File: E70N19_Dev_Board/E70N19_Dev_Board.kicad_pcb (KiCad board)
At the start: 2 copper layers, 71 parts, among them J1 USB_microB_2040002-1, J2 Battery 1x2, J3 JTAGSEL_JUMPER 1x3, J4 UART_PROG 1x2, J5 ERASE_JUMPER 1x3, J6 ARM-Cortex-Debug-10, J7 CAN 1x2, J8 Conn_02x15_Counter_Clockwise, J9 Conn_02x15_Counter_Clockwise, SW1 NRST_BUTTON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

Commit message: Added debug LEDs
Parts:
- added D4: LED_Small, LEDs:LED_0805, F.Cu at (142.2, 90.3)
- added D5: LED_Small, LEDs:LED_0805, F.Cu at (138.4, 90.3)
- added D6: LED_Small, LEDs:LED_0805, F.Cu at (146.1, 90.3)
- added R16: 1K, Resistors_SMD:R_0603, F.Cu at (142.2, 94.5)
- added R17: 1K, Resistors_SMD:R_0603, F.Cu at (138.4, 94.5)
- added R18: 1K, Resistors_SMD:R_0603, F.Cu at (146.1, 94.5)
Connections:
- C1 pad 1: Net-(C1-Pad1) -> /VBUS
- C2 pad 1: Net-(C1-Pad1) -> /VBUS
- C4 pad 1: Net-(C1-Pad1) -> /VBUS
- D1 pad 2: Net-(C1-Pad1) -> /VBUS
- J1 pad 1: Net-(C1-Pad1) -> /VBUS
- J8 pad 24: /PD24 -> /PD27
- J8 pad 25: /PD25 -> /PD31
- J8 pad 26: /PD26 -> GND
- J8 pad 27: /PD27 -> GND
- J8 pad 28: /PD31 -> GND
- J8 pad 29: Net-(J8-Pad29) -> /VBUS
- J8 pad 30: Net-(J8-Pad30) -> +3V3
- U1 pad 4: Net-(C1-Pad1) -> /VBUS
- U2 pad 8: Net-(C1-Pad1) -> /VBUS
- U4 pad 35: /PD25 -> Net-(D5-Pad2)
- U4 pad 36: /PD26 -> Net-(D6-Pad2)
- U4 pad 37: /PD24 -> Net-(D4-Pad2)

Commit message: Initial routing
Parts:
- moved J4 42.2 mm to (150.9, 72.4), turned to 180 degrees
- moved J8 36.9 mm to (92.2, 98.6), turned to 90 degrees
- moved R13 34.2 mm to (125.7, 43.2)
- moved D1 32.7 mm to (88.9, 37.5), turned to 270 degrees
- moved C26 32.3 mm to (103.1, 77.0), turned to 270 degrees
- moved J7 31.0 mm to (88.4, 76.2)
- moved D3 29.6 mm to (122.0, 43.2), turned to 180 degrees
- moved R1 29.3 mm to (94.2, 32.5), turned to 180 degrees
- moved R11 28.9 mm to (140.2, 59.4), turned to 315 degrees
- moved C3 28.8 mm to (90.4, 32.8), turned to 90 degrees
- moved U6 27.9 mm to (97.4, 76.8)
- moved C5 27.6 mm to (117.9, 41.1)
- moved U3 24.7 mm to (113.9, 44.0)
- moved C27 24.6 mm to (151.4, 104.6), turned to 90 degrees
- moved R8 24.1 mm to (149.9, 95.8), turned to 270 degrees
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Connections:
- net Net-(R14-Pad1) renamed /D_N
- net Net-(R15-Pad1) renamed /D_P
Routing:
- net +3V3: track 0.00 -> 61.2 mm
- net Net-(C3-Pad1): track 0.00 -> 55.8 mm
- net Net-(C14-Pad1): track 0.00 -> 55.2 mm
- net /VBUS: track 0.00 -> 51.9 mm
- net Net-(FP1-Pad8): track 0.00 -> 51.3 mm
- net Net-(FP1-Pad7): track 0.00 -> 50.3 mm, vias 0 -> 4
- net Net-(J5-Pad3): track 0.00 -> 38.1 mm, vias 0 -> 4
- net /D_N: track 0.00 -> 36.0 mm
- net /D_P: track 0.00 -> 35.6 mm
- net /TMS: track 0.00 -> 34.9 mm
- net /NRST: track 0.00 -> 32.0 mm, vias 0 -> 4
- net /CAN_RX: track 0.00 -> 31.6 mm, vias 0 -> 2
- net Net-(C29-Pad1): track 0.00 -> 29.4 mm
- net /CAN_TX: track 0.00 -> 27.2 mm
- net /TCK: track 0.00 -> 24.7 mm
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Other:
- board outline added: 100 x 100 mm
- net class Default: trace_width 0.1524 -> 0.2032

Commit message: Beginning to route
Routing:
- net +3V3: track 61.2 -> 431.4 mm, vias 0 -> 6
- net GND: track 7.59 -> 113.1 mm, vias 0 -> 48
- net /VBUS: track 51.9 -> 150.8 mm, vias 0 -> 2
- net /PA27: track 0.00 -> 7.97 mm
- net /PD18: track 0.00 -> 7.53 mm
- net /PA12: track 0.00 -> 6.86 mm
- net /PD19: track 0.00 -> 6.77 mm
- net /CAN_RX: track 31.6 -> 32.7 mm
- net Net-(J4-Pad1): track 17.8 -> 18.7 mm, vias 0 -> 2
- net Net-(FP1-Pad8): track 51.3 -> 52.0 mm, vias 0 -> 2
- added copper zone on B.Cu, net GND

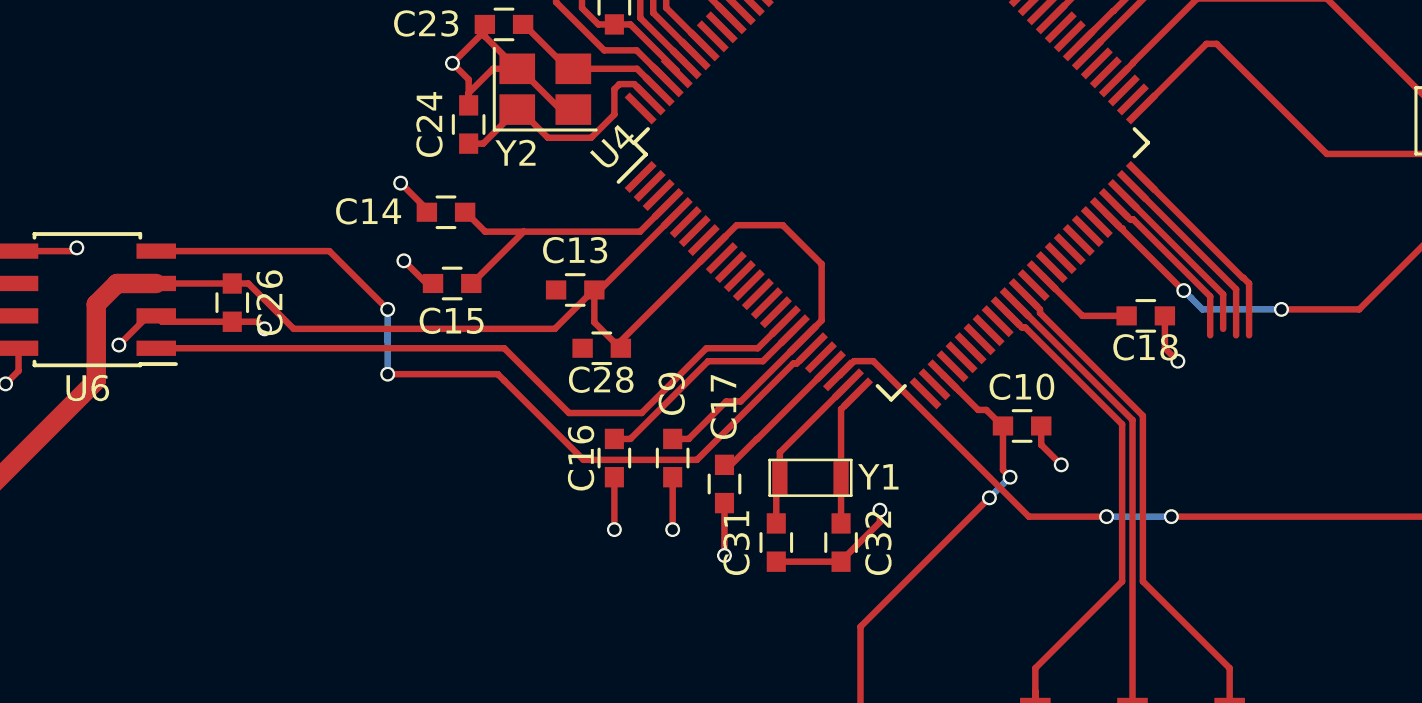
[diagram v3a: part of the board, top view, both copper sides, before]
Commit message: More excape routing
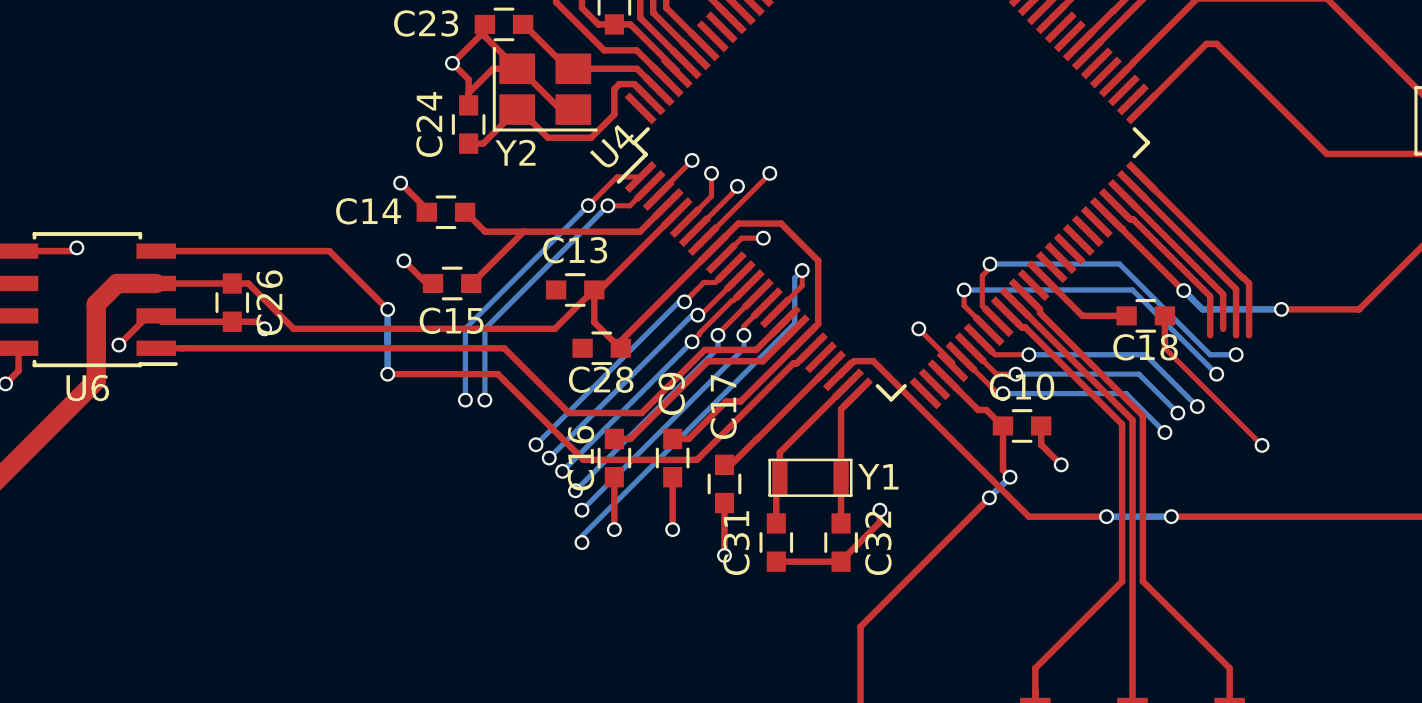
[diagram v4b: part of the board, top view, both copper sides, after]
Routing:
- net GND: track 113.1 -> 132.1 mm, vias 48 -> 54
- net /PA17: track 0.00 -> 16.3 mm, vias 0 -> 2
- net /PA14: track 0.00 -> 13.7 mm, vias 0 -> 2
- net /PA15: track 0.00 -> 13.3 mm, vias 0 -> 2
- net /PD0: track 0.00 -> 12.1 mm, vias 0 -> 2
- net /PD31: track 0.00 -> 11.6 mm, vias 0 -> 2
- net /PA18: track 0.00 -> 11.1 mm, vias 0 -> 2
- net /PA19: track 0.00 -> 10.7 mm, vias 0 -> 2
- net /PB1: track 0.00 -> 10.5 mm, vias 0 -> 2
- net /PB0: track 0.00 -> 10.4 mm, vias 0 -> 2
- net /PA20: track 0.00 -> 10.4 mm, vias 0 -> 2
- net /PD27: track 0.00 -> 9.63 mm, vias 0 -> 2
- net /PA16: track 0.00 -> 9.19 mm, vias 0 -> 2
- net /PA23: track 0.00 -> 9.18 mm, vias 0 -> 2

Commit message: Updated with new schematic
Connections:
- J8 pad 1: /PD0 -> /PD9
- J8 pad 10: /PD9 -> /PD3
- J8 pad 11: /PD10 -> /PD2
- J8 pad 12: /PD11 -> /PD1
- J8 pad 13: /PD12 -> /PB13
- J8 pad 14: /PD13 -> /PD0
- J8 pad 15: /PD14 -> /PD31
- J8 pad 16: /PD15 -> /PB1
- J8 pad 17: /PD16 -> /PB0
- J8 pad 18: /PD17 -> /PA20
- J8 pad 19: /PD18 -> /PA19
- J8 pad 2: /PD1 -> /PA28
- J8 pad 20: /PD19 -> /PA18
- J8 pad 21: /PD20 -> /PA17
- J8 pad 22: /PD21 -> /PA21
- J8 pad 23: /PD22 -> /PA22
- J8 pad 24: /PD27 -> /PA13
- J8 pad 25: /PD31 -> /PA16
- J8 pad 3: /PD2 -> /PD8
- J8 pad 4: /PD3 -> /PA30
- J8 pad 5: /PD4 -> /PA31
- J8 pad 6: /PD5 -> /PD7
- J8 pad 8: /PD7 -> /PD5
- J8 pad 9: /PD8 -> /PD4
- J9 pad 1: /PA0 -> /PD15
- J9 pad 10: /PA14 -> /PD13
- J9 pad 11: /PA15 -> /PD14
- J9 pad 12: /PA16 -> /PD16
- J9 pad 13: /PA17 -> /PA4
- J9 pad 14: /PA18 -> /PD17
- J9 pad 15: /PA19 -> /PA5
- J9 pad 16: /PA20 -> /PA27
- J9 pad 17: /PA21 -> /PD18
- J9 pad 18: /PA22 -> /PA12
- J9 pad 19: /PA23 -> /PD19
- J9 pad 2: /PA1 -> /PA0
- J9 pad 20: /PA24 -> /PD20
- J9 pad 21: /PA25 -> /PA11
- J9 pad 22: /PA26 -> /PD21
- J9 pad 23: /PA27 -> /PA26
- J9 pad 24: /PA28 -> /PD22
- J9 pad 25: /PA30 -> /PA25
- J9 pad 26: /PA31 -> /PA24
- J9 pad 27: /PB0 -> /PA14
- J9 pad 28: /PB1 -> /PA15
- J9 pad 29: /PB13 -> /PD27
- J9 pad 3: /PA2 -> /PD10
- J9 pad 30: Net-(J9-Pad30) -> /PA23
- J9 pad 4: /PA3 -> /PA1
- J9 pad 5: /PA4 -> /PD11
- J9 pad 7: /PA11 -> /PA2
- J9 pad 8: /PA12 -> /PD12
- J9 pad 9: /PA13 -> /PA3

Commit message: Finishing double layer board
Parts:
- added G***: LOGO, footprints:Byron-Face-2, B.Cu at (101.6, 67.3)
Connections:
- J8 pad 1: /PD9 -> Net-(J8-Pad1)
- J8 pad 10: /PD3 -> /PB1
- J8 pad 11: /PD2 -> Net-(J8-Pad11)
- J8 pad 12: /PD1 -> /PB0
- J8 pad 13: /PB13 -> Net-(J8-Pad13)
- J8 pad 14: /PD0 -> /PA20
- J8 pad 15: /PD31 -> Net-(J8-Pad15)
- J8 pad 16: /PB1 -> /PA19
- J8 pad 17: /PB0 -> Net-(J8-Pad17)
- J8 pad 18: /PA20 -> /PA18
- J8 pad 19: /PA19 -> Net-(J8-Pad19)
- J8 pad 2: /PA28 -> /PD0
- J8 pad 20: /PA18 -> /PA17
- J8 pad 21: /PA17 -> Net-(J8-Pad21)
- J8 pad 22: /PA21 -> Net-(J8-Pad22)
- J8 pad 23: /PA22 -> Net-(J8-Pad23)
- J8 pad 24: /PA13 -> Net-(J8-Pad24)
- J8 pad 25: /PA16 -> Net-(J8-Pad25)
- J8 pad 3: /PD8 -> Net-(J8-Pad3)
- J8 pad 4: /PA30 -> /PD31
- J8 pad 5: /PA31 -> Net-(J8-Pad5)
- J8 pad 6: /PD7 -> Net-(J8-Pad6)
- J8 pad 7: /PD6 -> Net-(J8-Pad7)
- J8 pad 8: /PD5 -> Net-(J8-Pad8)
- J8 pad 9: /PD4 -> Net-(J8-Pad9)
- J9 pad 1: /PD15 -> /PA27
- J9 pad 10: /PD13 -> Net-(J9-Pad10)
- J9 pad 11: /PD14 -> /PA15
- J9 pad 12: /PD16 -> Net-(J9-Pad12)
- J9 pad 13: /PA4 -> /PD27
- J9 pad 14: /PD17 -> Net-(J9-Pad14)
- J9 pad 15: /PA5 -> /PA23
- J9 pad 16: /PA27 -> Net-(J9-Pad16)
- J9 pad 17: /PD18 -> /PA16
- J9 pad 18: /PA12 -> Net-(J9-Pad18)
- J9 pad 19: /PD19 -> Net-(J9-Pad19)
- J9 pad 2: /PA0 -> Net-(J9-Pad2)
- J9 pad 20: /PD20 -> Net-(J9-Pad20)
- J9 pad 21: /PA11 -> Net-(J9-Pad21)
- J9 pad 22: /PD21 -> Net-(J9-Pad22)
- J9 pad 23: /PA26 -> Net-(J9-Pad23)
- J9 pad 24: /PD22 -> Net-(J9-Pad24)
- J9 pad 25: /PA25 -> Net-(J9-Pad25)
- J9 pad 26: /PA24 -> Net-(J9-Pad26)
- J9 pad 27: /PA14 -> Net-(J9-Pad27)
- J9 pad 28: /PA15 -> Net-(J9-Pad28)
- J9 pad 29: /PD27 -> Net-(J9-Pad29)
- J9 pad 3: /PD10 -> /PA14
- J9 pad 30: /PA23 -> Net-(J9-Pad30)
- J9 pad 4: /PA1 -> Net-(J9-Pad4)
- J9 pad 5: /PD11 -> /PD18
- J9 pad 6: /PA5 -> Net-(J9-Pad6)
- J9 pad 7: /PA2 -> /PA12
- J9 pad 8: /PD12 -> Net-(J9-Pad8)
- J9 pad 9: /PA3 -> /PD19
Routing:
- net Net-(C14-Pad1): track 55.2 -> 102.7 mm, vias 0 -> 4
- net /PA27: track 7.97 -> 49.5 mm
- net /PA12: track 6.86 -> 48.3 mm
- net /PD18: track 7.53 -> 48.7 mm
- net /PA14: track 13.7 -> 54.7 mm
- net /PD19: track 6.77 -> 47.2 mm
- net /PA15: track 13.3 -> 52.9 mm
- net /PA23: track 9.18 -> 43.3 mm
- net /PD27: track 9.63 -> 43.7 mm
- net /PA16: track 9.19 -> 42.7 mm
- net /PD0: track 12.1 -> 39.7 mm
- net /PD31: track 11.6 -> 38.0 mm
- net /PB1: track 10.5 -> 30.0 mm
- net /PB0: track 10.4 -> 27.8 mm
- net /PA20: track 10.4 -> 26.4 mm
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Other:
- board size 100 x 100 mm -> 88.9 x 83.8 mm
- board text added: "ATSAME70N19 Dev Board Rev.1 Byron Wasti and Alexander Hoppe Ecelectronics Fall '17 Olin College of Engineering"

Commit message: Adding Hoppe's face
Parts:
- added G***: LOGO, eclectronics:hoppe, B.Cu at (128.9, 70.5)
- added G***: LOGO, eclectronics:hoppe, F.Cu at (129.5, 71.1)

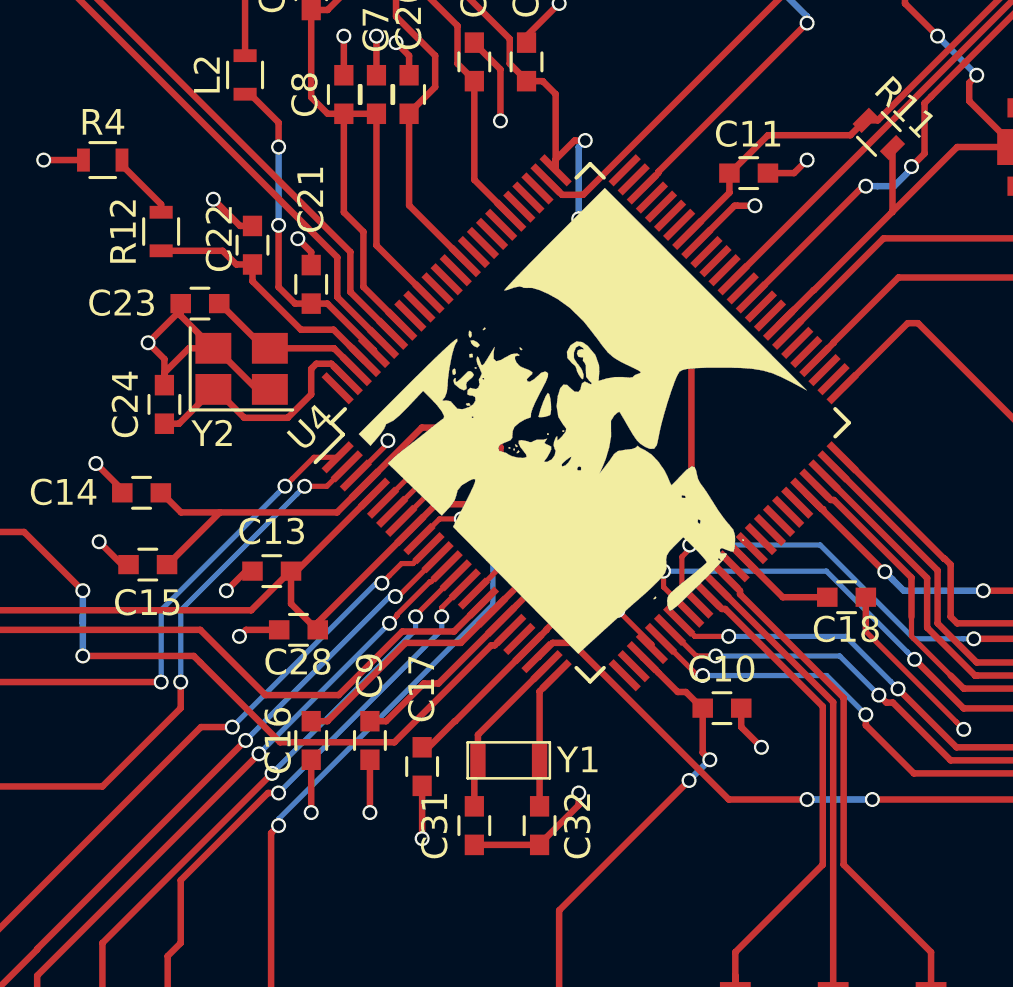
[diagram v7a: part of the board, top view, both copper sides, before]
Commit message: Fixing unconnected ground nets
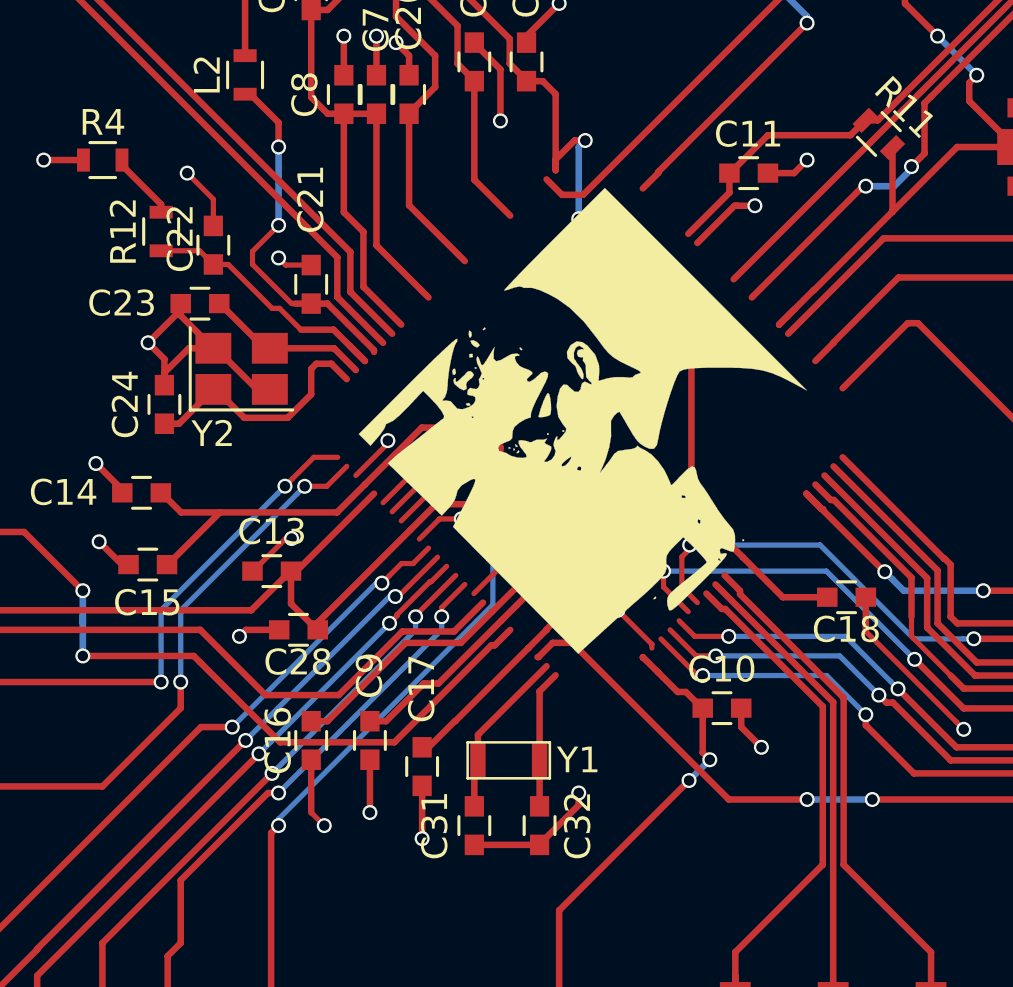
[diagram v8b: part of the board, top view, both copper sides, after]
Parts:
- removed U4: ATSAME70N19, Housings_QFP:LQFP-100_14x14mm_Pitch0.5mm
- moved C22 1.52 mm to (114.3, 63.8)
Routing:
- net (no net): track 0.00 -> 17.0 mm, vias 0 -> 7
- net GND: track 143.6 -> 128.6 mm, vias 58 -> 51
- net Net-(C21-Pad1): track 13.0 -> 13.9 mm
